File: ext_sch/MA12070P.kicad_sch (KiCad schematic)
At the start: 49 parts, among them J7 Screw Term.

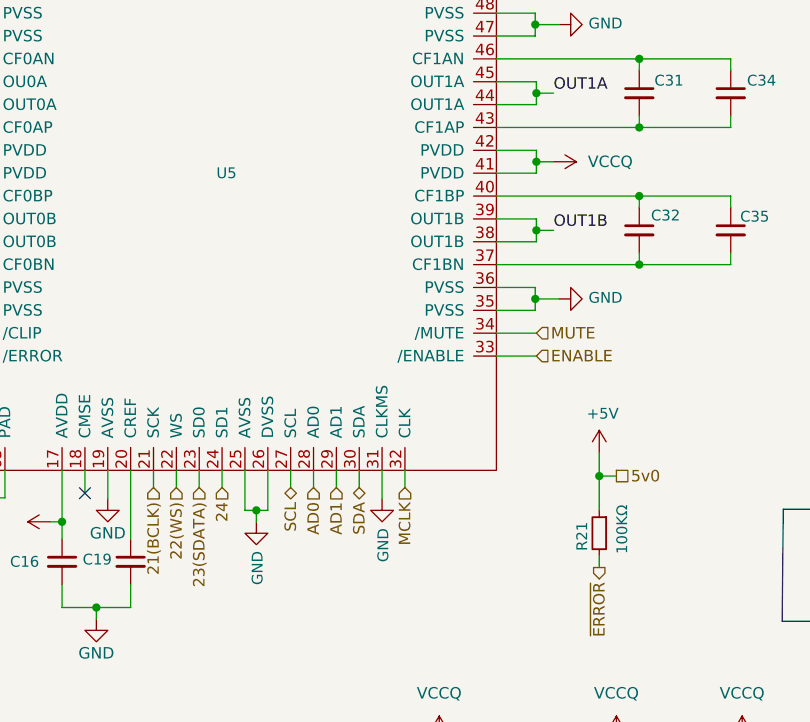
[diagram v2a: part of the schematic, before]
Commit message: Lastest revised files. Loads more DC protection now, thanks to @feelfreelinux
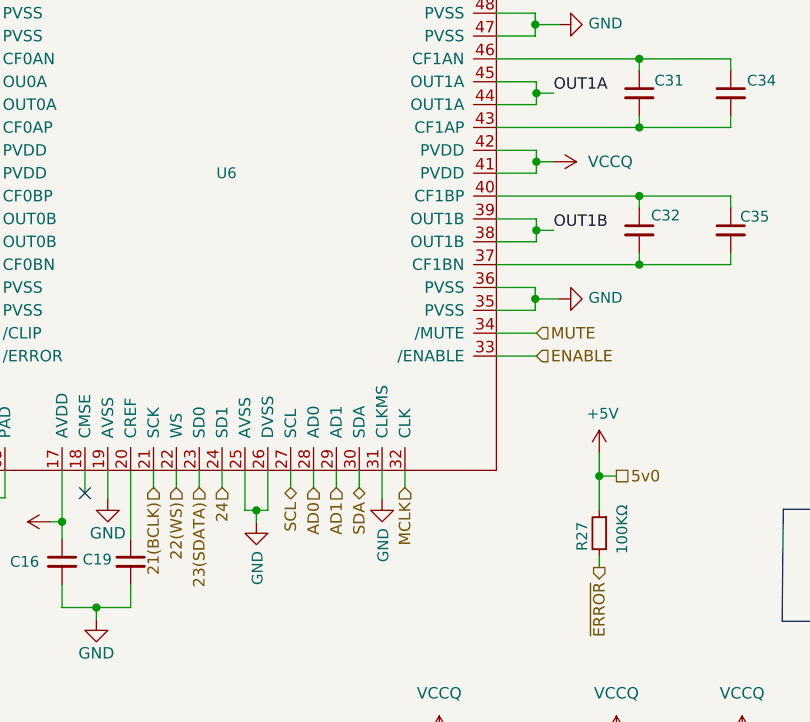
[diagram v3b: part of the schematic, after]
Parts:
- renumbered R21 to R27, U5 to U6
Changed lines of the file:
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@@
   (symbol (lib_id "power:GND") (at 382.651 180.34 270) (mirror x) (unit 1)
     (in_bom yes) (on_board yes)
-    (property "Reference" "#PWR080" (id 0) (at 376.301 180.34 0)
+    (property "Reference" "#PWR083" (id 0) (at 376.301 180.34 0)
       (effects (font (size 1.2 1.2)) hide)
     )
@@
   (symbol (lib_id "power:GND") (at 300.482 137.287 0) (unit 1)
     (in_bom yes) (on_board yes)
-    (property "Reference" "#PWR064" (id 0) (at 300.482 143.637 0)
+    (property "Reference" "#PWR067" (id 0) (at 300.482 143.637 0)
       (effects (font (size 1.2 1.2)) hide)
     )
@@
   (symbol (lib_id "power:GND") (at 341.63 165.735 0) (unit 1)
     (in_bom yes) (on_board yes)
-    (property "Reference" "#PWR076" (id 0) (at 341.63 172.085 0)
+    (property "Reference" "#PWR079" (id 0) (at 341.63 172.085 0)
       (effects (font (size 1.2 1.2)) hide)
     )
@@
   (symbol (lib_id "muVoxSyms:MA12070P") (at 289.56 172.085 0) (unit 1)
     (in_bom yes) (on_board yes)
-    (property "Reference" "U5" (id 0) (at 297.815 196.215 0)
+    (property "Reference" "U6" (id 0) (at 297.815 196.215 0)
       (effects (font (size 1.2 1.2)) (justify left))
     )
@@
   (symbol (lib_id "power:+5V") (at 279.4 234.95 90) (unit 1)
     (in_bom yes) (on_board yes)
-    (property "Reference" "#PWR060" (id 0) (at 283.21 234.95 0)
+    (property "Reference" "#PWR063" (id 0) (at 283.21 234.95 0)
       (effects (font (size 1.2 1.2)) hide)
     )
@@
   (symbol (lib_id "power:GND") (at 300.99 152.4 180) (unit 1)
     (in_bom yes) (on_board yes)
-    (property "Reference" "#PWR065" (id 0) (at 300.99 146.05 0)
+    (property "Reference" "#PWR068" (id 0) (at 300.99 146.05 0)
       (effects (font (size 1.2 1.2)) hide)
     )
@@
   (symbol (lib_id "power:VCCQ") (at 356.235 259.08 0) (unit 1)
     (in_bom yes) (on_board yes) (fields_autoplaced)
-    (property "Reference" "#PWR079" (id 0) (at 356.235 262.89 0)
+    (property "Reference" "#PWR082" (id 0) (at 356.235 262.89 0)
       (effects (font (size 1.27 1.27)) hide)
     )
@@
   (symbol (lib_id "power:VCCQ") (at 264.16 194.945 90) (mirror x) (unit 1)
     (in_bom yes) (on_board yes) (fields_autoplaced)
-    (property "Reference" "#PWR058" (id 0) (at 267.97 194.945 0)
+    (property "Reference" "#PWR061" (id 0) (at 267.97 194.945 0)
       (effects (font (size 1.27 1.27)) hide)
     )
@@
   (symbol (lib_id "power:GND") (at 285.75 232.41 0) (unit 1)
     (in_bom yes) (on_board yes)
-    (property "Reference" "#PWR062" (id 0) (at 285.75 238.76 0)
+    (property "Reference" "#PWR065" (id 0) (at 285.75 238.76 0)
       (effects (font (size 1.27 1.27)) hide)
     )
@@
   (symbol (lib_id "power:GND") (at 394.97 272.415 0) (unit 1)
     (in_bom yes) (on_board yes)
-    (property "Reference" "#PWR083" (id 0) (at 394.97 278.765 0)
+    (property "Reference" "#PWR086" (id 0) (at 394.97 278.765 0)
       (effects (font (size 1.2 1.2)) hide)
     )
@@
   (symbol (lib_id "power:GND") (at 335.915 179.705 90) (unit 1)
     (in_bom yes) (on_board yes)
-    (property "Reference" "#PWR072" (id 0) (at 342.265 179.705 0)
+    (property "Reference" "#PWR075" (id 0) (at 342.265 179.705 0)
       (effects (font (size 1.2 1.2)) hide)
     )
@@
   (symbol (lib_id "Device:R_Small") (at 340.36 236.22 0) (mirror y) (unit 1)
     (in_bom yes) (on_board yes)
-    (property "Reference" "R21" (id 0) (at 338.455 234.95 90)
+    (property "Reference" "R27" (id 0) (at 338.455 234.95 90)
       (effects (font (size 1.2 1.2)) (justify right))
     )
@@
   (symbol (lib_id "power:VDC") (at 384.175 259.08 0) (unit 1)
     (in_bom yes) (on_board yes)
-    (property "Reference" "#PWR082" (id 0) (at 384.175 261.62 0)
+    (property "Reference" "#PWR085" (id 0) (at 384.175 261.62 0)
       (effects (font (size 1.27 1.27)) hide)
     )
@@
   (symbol (lib_id "power:GND") (at 263.525 179.705 270) (mirror x) (unit 1)
     (in_bom yes) (on_board yes)
-    (property "Reference" "#PWR056" (id 0) (at 257.175 179.705 0)
+    (property "Reference" "#PWR059" (id 0) (at 257.175 179.705 0)
       (effects (font (size 1.2 1.2)) hide)
     )
@@
   (symbol (lib_id "power:GND") (at 302.26 234.95 0) (unit 1)
     (in_bom yes) (on_board yes)
-    (property "Reference" "#PWR066" (id 0) (at 302.26 241.3 0)
+    (property "Reference" "#PWR069" (id 0) (at 302.26 241.3 0)
       (effects (font (size 1.2 1.2)) hide)
     )
@@
   (symbol (lib_id "power:GND") (at 342.265 272.415 0) (unit 1)
     (in_bom yes) (on_board yes)
-    (property "Reference" "#PWR078" (id 0) (at 342.265 278.765 0)
+    (property "Reference" "#PWR081" (id 0) (at 342.265 278.765 0)
       (effects (font (size 1.2 1.2)) hide)
     )
@@
   (symbol (lib_id "power:+5V") (at 304.8 151.765 0) (unit 1)
     (in_bom yes) (on_board yes)
-    (property "Reference" "#PWR067" (id 0) (at 304.8 155.575 0)
+    (property "Reference" "#PWR070" (id 0) (at 304.8 155.575 0)
       (effects (font (size 1.2 1.2)) hide)
     )
@@
   (symbol (lib_id "power:GND") (at 322.58 272.415 0) (unit 1)
     (in_bom yes) (on_board yes)
-    (property "Reference" "#PWR070" (id 0) (at 322.58 278.765 0)
+    (property "Reference" "#PWR073" (id 0) (at 322.58 278.765 0)
       (effects (font (size 1.2 1.2)) hide)
     )
@@
   (symbol (lib_id "power:GND") (at 382.651 215.265 270) (mirror x) (unit 1)
     (in_bom yes) (on_board yes)
-    (property "Reference" "#PWR081" (id 0) (at 376.301 215.265 0)
+    (property "Reference" "#PWR084" (id 0) (at 376.301 215.265 0)
       (effects (font (size 1.2 1.2)) hide)
     )
@@
   (symbol (lib_id "power:GND") (at 293.37 164.465 180) (unit 1)
     (in_bom yes) (on_board yes)
-    (property "Reference" "#PWR063" (id 0) (at 293.37 158.115 0)
+    (property "Reference" "#PWR066" (id 0) (at 293.37 158.115 0)
       (effects (font (size 1.2 1.2)) hide)
     )
@@
   (symbol (lib_id "power:VCC") (at 404.495 259.08 0) (unit 1)
     (in_bom yes) (on_board yes) (fields_autoplaced)
-    (property "Reference" "#PWR084" (id 0) (at 404.495 262.89 0)
+    (property "Reference" "#PWR087" (id 0) (at 404.495 262.89 0)
       (effects (font (size 1.27 1.27)) hide)
     )
@@
   (symbol (lib_id "power:GND") (at 284.48 245.745 0) (unit 1)
     (in_bom yes) (on_board yes)
-    (property "Reference" "#PWR061" (id 0) (at 284.48 252.095 0)
+    (property "Reference" "#PWR064" (id 0) (at 284.48 252.095 0)
       (effects (font (size 1.27 1.27)) hide)
     )
@@
   (symbol (lib_id "power:GND") (at 335.915 210.185 90) (unit 1)
     (in_bom yes) (on_board yes)
-    (property "Reference" "#PWR073" (id 0) (at 342.265 210.185 0)
+    (property "Reference" "#PWR076" (id 0) (at 342.265 210.185 0)
       (effects (font (size 1.2 1.2)) hide)
     )
@@
   (symbol (lib_id "power:GND") (at 316.23 232.41 0) (unit 1)
     (in_bom yes) (on_board yes)
-    (property "Reference" "#PWR068" (id 0) (at 316.23 238.76 0)
+    (property "Reference" "#PWR071" (id 0) (at 316.23 238.76 0)
       (effects (font (size 1.2 1.2)) hide)
     )
@@
   (symbol (lib_id "power:GND") (at 272.288 232.283 270) (unit 1)
     (in_bom yes) (on_board yes)
-    (property "Reference" "#PWR059" (id 0) (at 265.938 232.283 0)
+    (property "Reference" "#PWR062" (id 0) (at 265.938 232.283 0)
       (effects (font (size 1.27 1.27)) hide)
     )
@@
   (symbol (lib_id "power:VCCQ") (at 322.58 259.08 0) (unit 1)
     (in_bom yes) (on_board yes) (fields_autoplaced)
-    (property "Reference" "#PWR069" (id 0) (at 322.58 262.89 0)
+    (property "Reference" "#PWR072" (id 0) (at 322.58 262.89 0)
       (effects (font (size 1.27 1.27)) hide)
     )
@@
   (symbol (lib_id "power:VCCQ") (at 335.28 194.945 270) (unit 1)
     (in_bom yes) (on_board yes) (fields_autoplaced)
-    (property "Reference" "#PWR071" (id 0) (at 331.47 194.945 0)
+    (property "Reference" "#PWR074" (id 0) (at 331.47 194.945 0)
       (effects (font (size 1.27 1.27)) hide)
     )
@@
   (symbol (lib_id "power:GND") (at 263.525 210.185 270) (mirror x) (unit 1)
     (in_bom yes) (on_board yes)
-    (property "Reference" "#PWR057" (id 0) (at 257.175 210.185 0)
+    (property "Reference" "#PWR060" (id 0) (at 257.175 210.185 0)
       (effects (font (size 1.2 1.2)) hide)
     )
@@
   (symbol (lib_id "power:VCCQ") (at 342.265 259.08 0) (unit 1)
     (in_bom yes) (on_board yes) (fields_autoplaced)
-    (property "Reference" "#PWR077" (id 0) (at 342.265 262.89 0)
+    (property "Reference" "#PWR080" (id 0) (at 342.265 262.89 0)
       (effects (font (size 1.27 1.27)) hide)
     )
@@
   (symbol (lib_id "power:+5V") (at 341.63 148.59 0) (unit 1)
     (in_bom yes) (on_board yes)
-    (property "Reference" "#PWR075" (id 0) (at 341.63 152.4 0)
+    (property "Reference" "#PWR078" (id 0) (at 341.63 152.4 0)
       (effects (font (size 1.2 1.2)) hide)
     )
@@
   (symbol (lib_id "power:+5V") (at 340.36 227.33 0) (unit 1)
     (in_bom yes) (on_board yes)
-    (property "Reference" "#PWR074" (id 0) (at 340.36 231.14 0)
-      (effects (font (size 1.2 1.2)) hide)
-    )
+    (property "Reference" "#PWR077" (id 0) (at 340.36 231.14 0)
+      (effects (font (size 1.2 1.2)) hide)
+    )

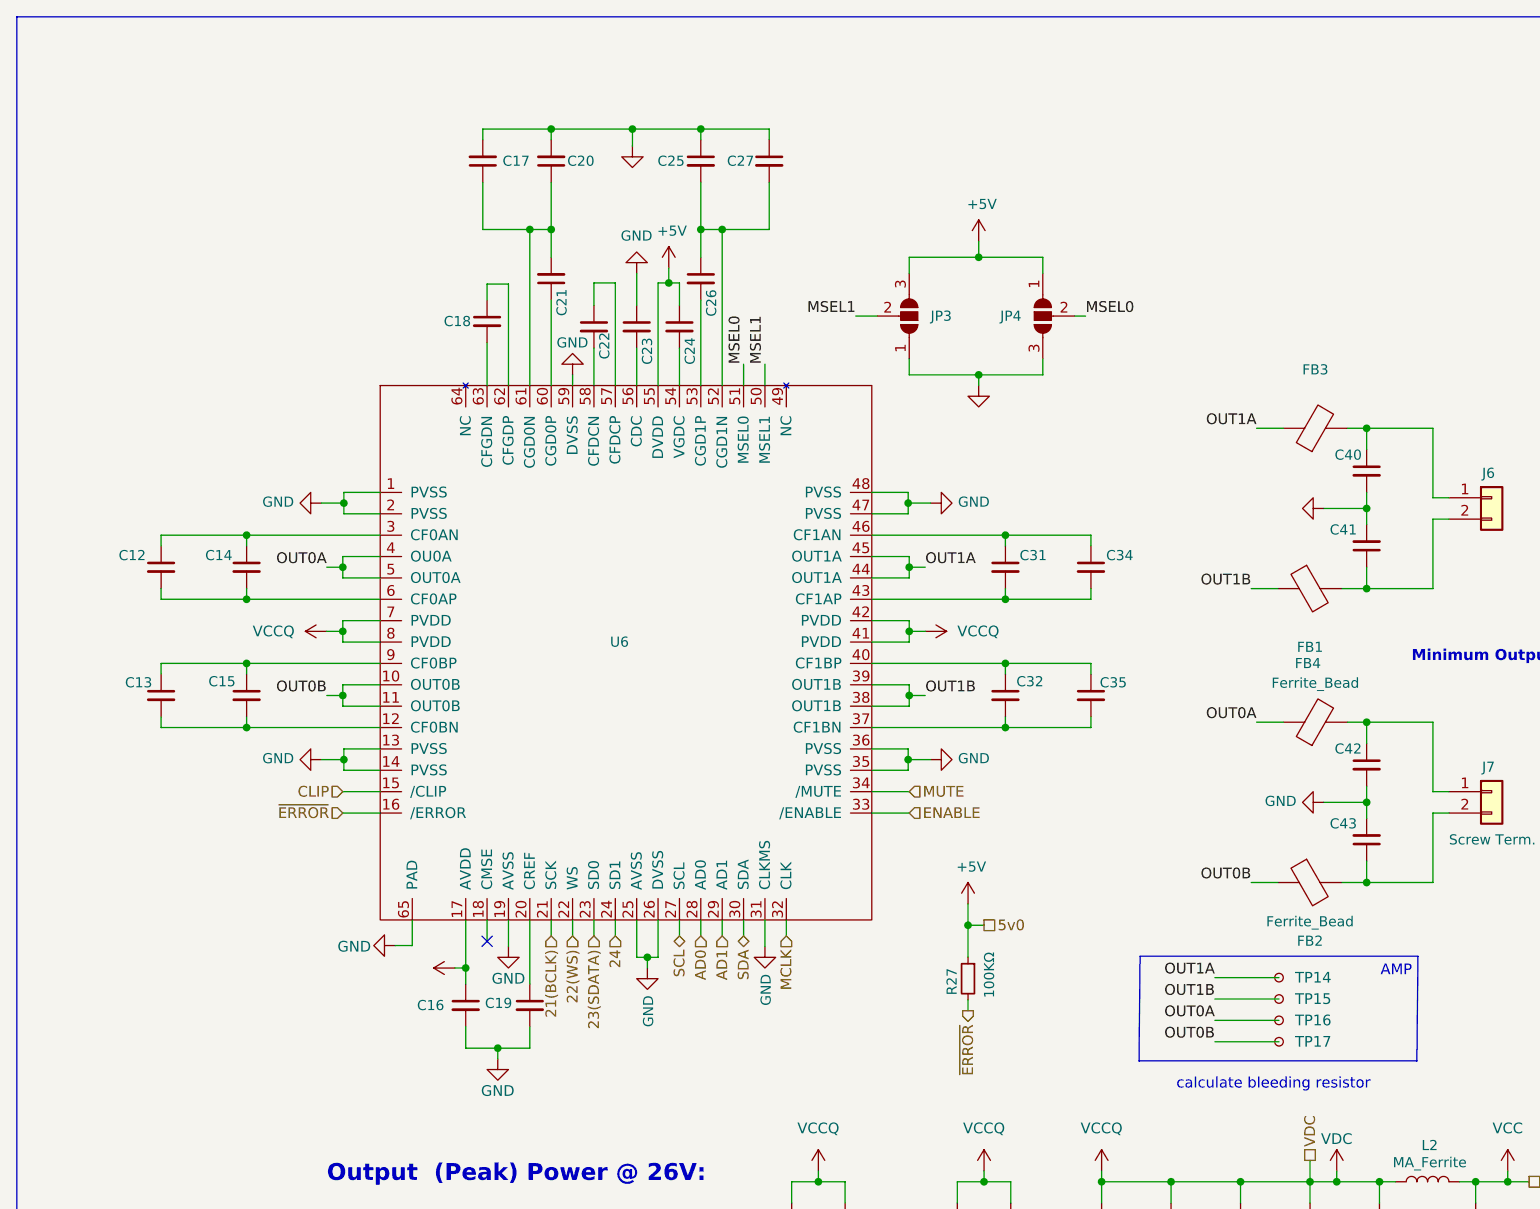
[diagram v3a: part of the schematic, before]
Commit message: feat: new schematic, adjust LCSC part numbers
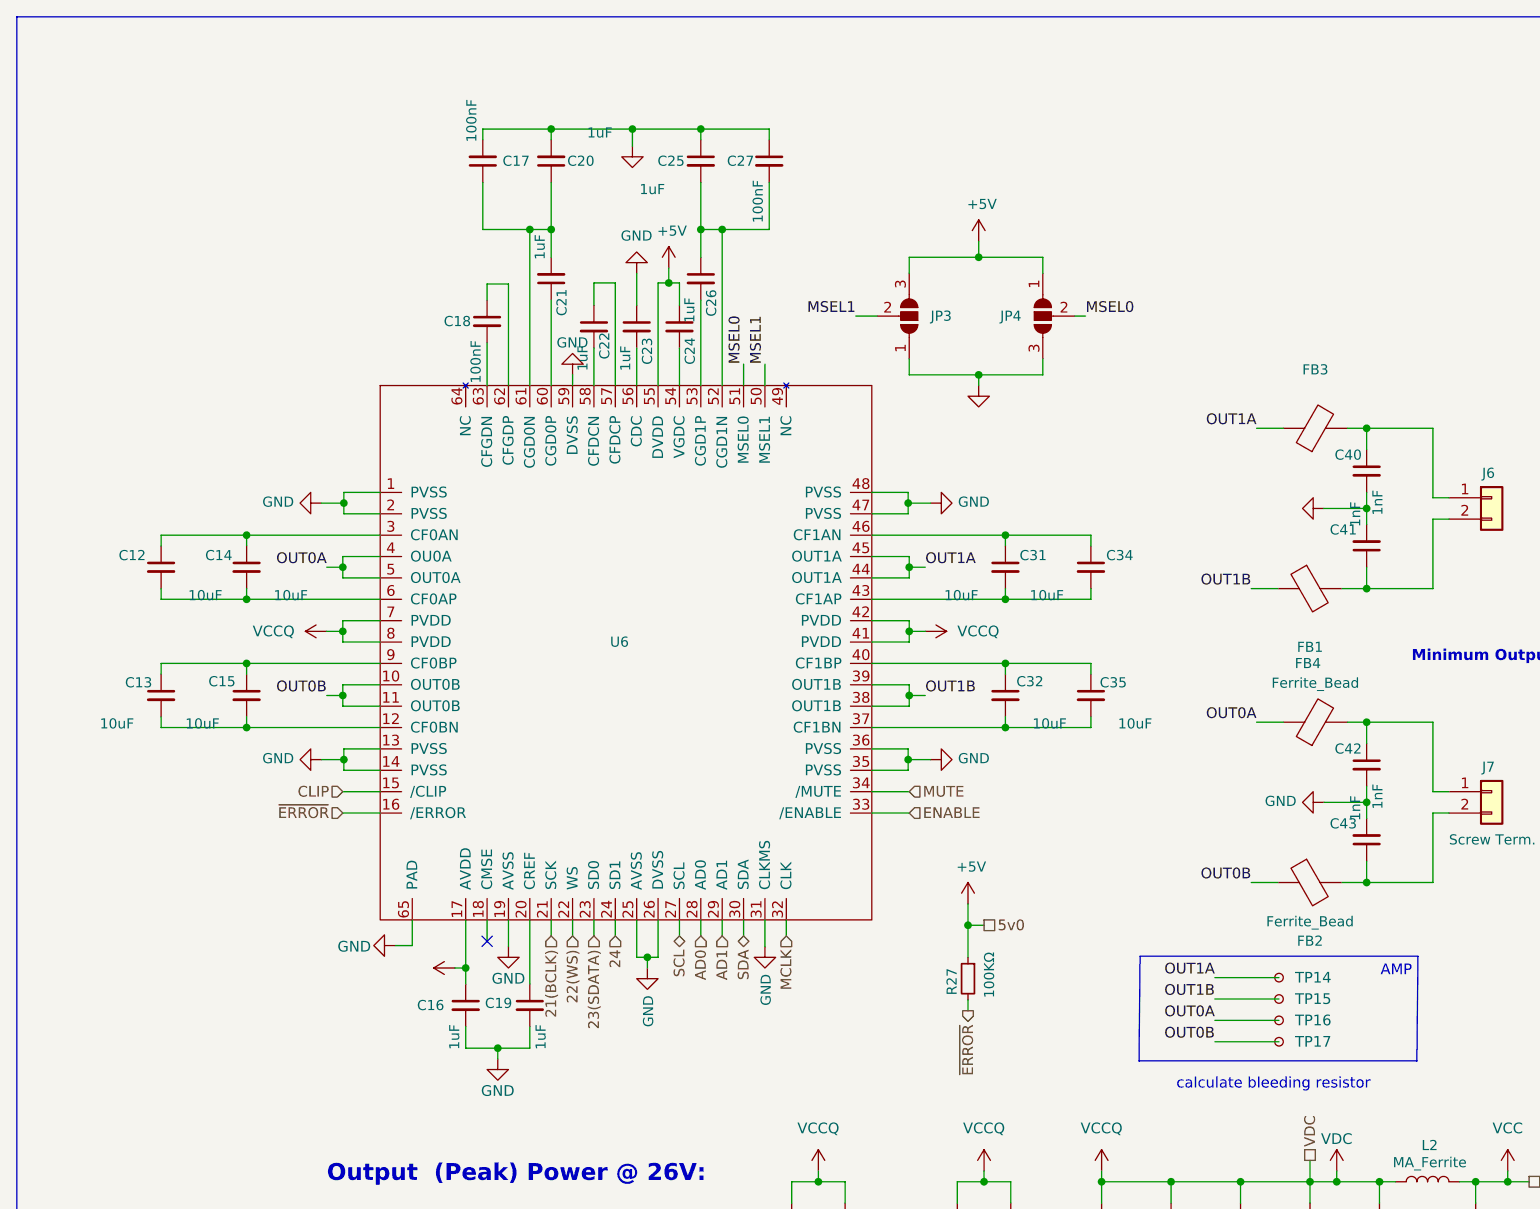
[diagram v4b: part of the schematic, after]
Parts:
- C12, C13, C14, C15, C31, C32, C34, C35: LCSC C162422 -> C15850
- C16, C19, C21, C22, C23, C24, C26: LCSC C157684 -> C15849
- C20, C25, C28, C30: LCSC C318694 -> C519978
- C40, C41, C42, C43: LCSC C44369 -> C100040
- C44, C45: LCSC C21122 -> C106222
